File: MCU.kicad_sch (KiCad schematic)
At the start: 45 parts, among them J15 Conn_01x08, J16 Conn_02x04_Odd_Even, J17 TFC-103-01-F-D, J19 TFC-103-01-F-D, Q13 SI2300, SW1 SW_Push_Dual, SW2 SW_Push_Dual, SW3 SW_DIP_x08, U15 MCP1700-3302E_SOT23, U16 CD74HC4067M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

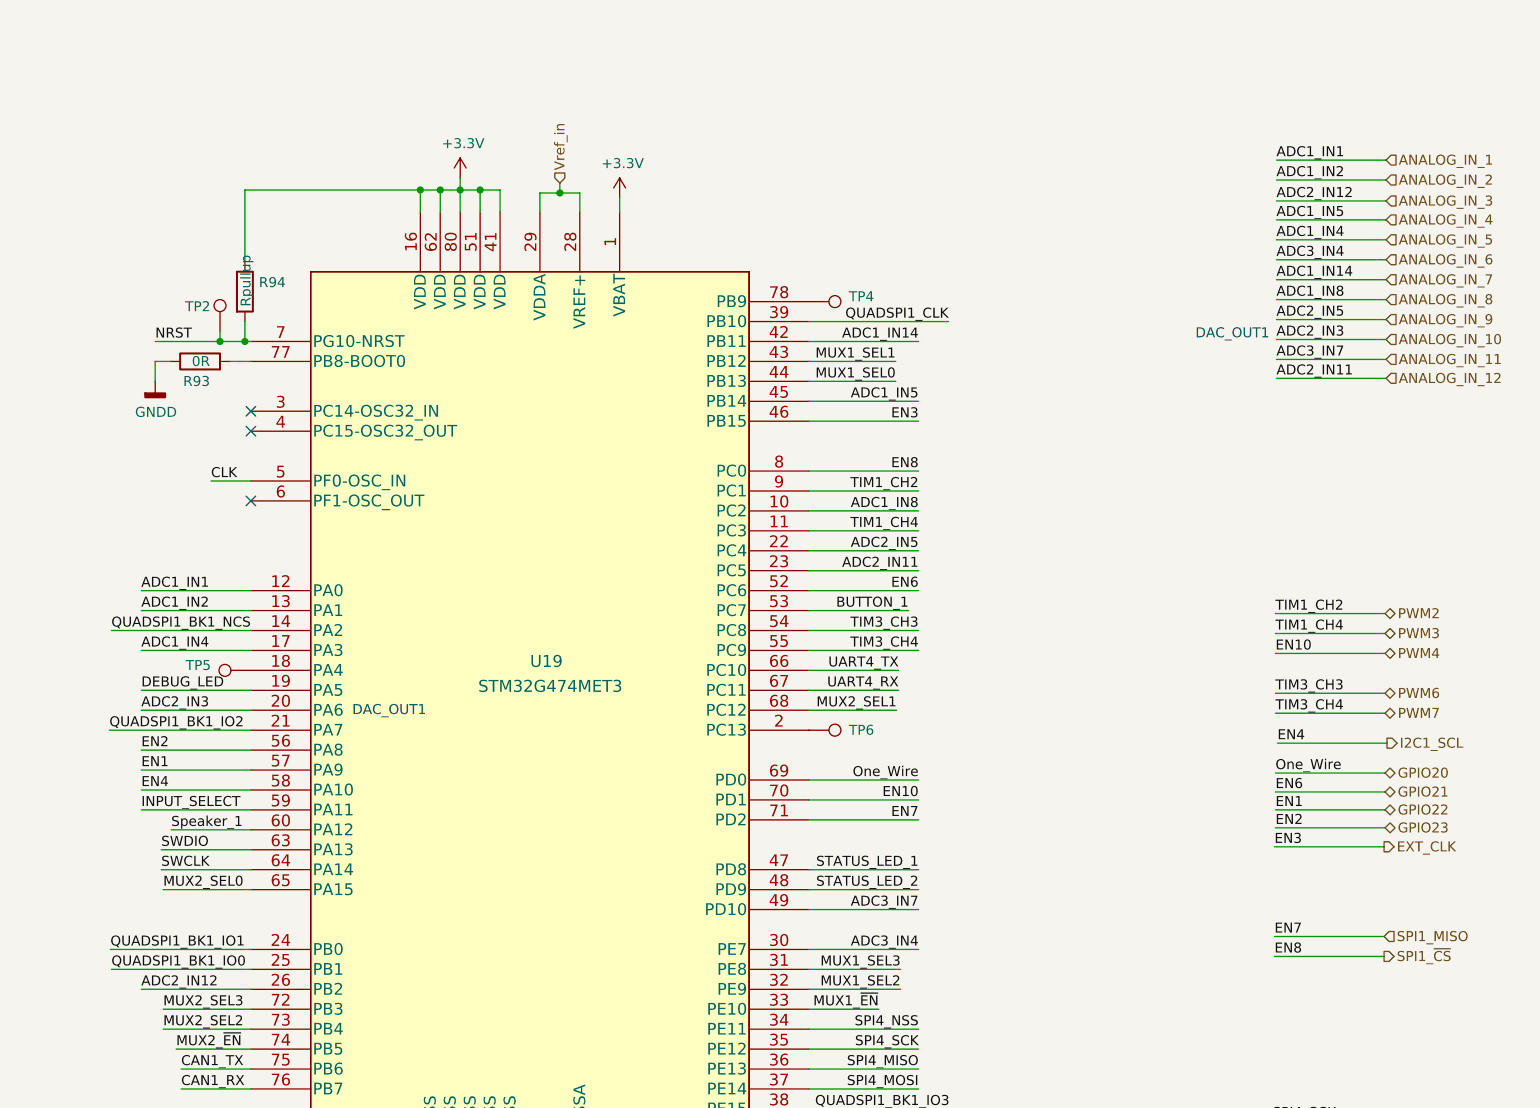
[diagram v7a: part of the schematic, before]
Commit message: Routing complete. Stitching missing
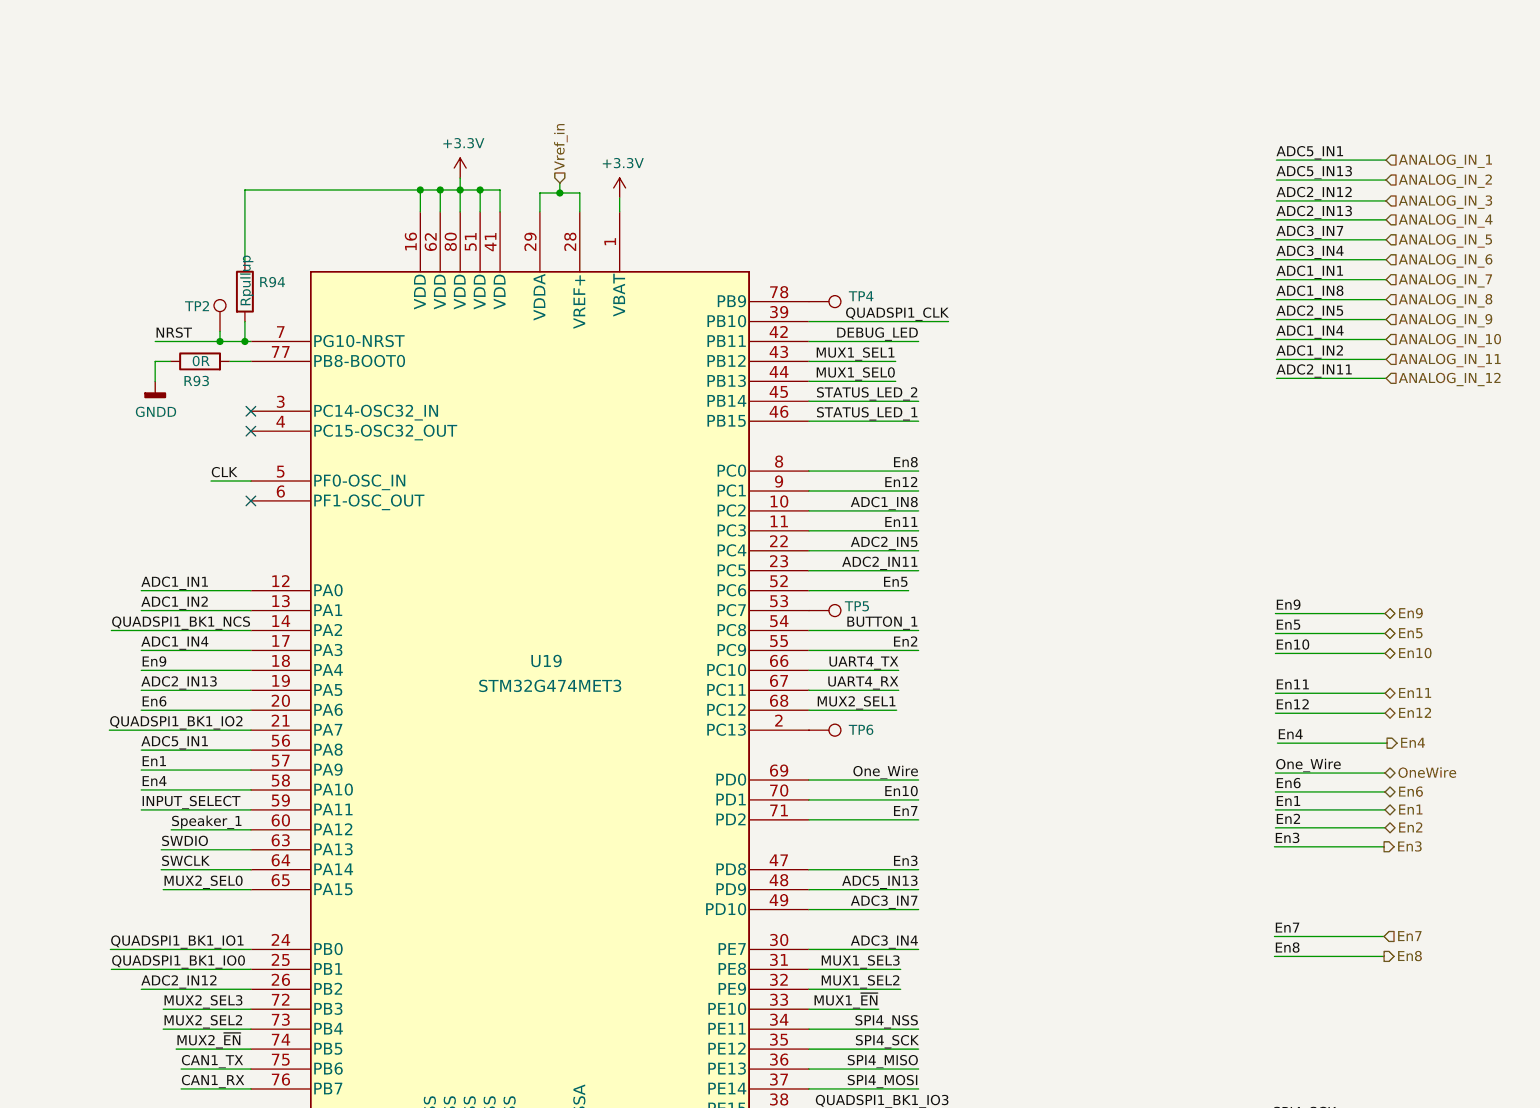
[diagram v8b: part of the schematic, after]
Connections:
- net EXT_CLK is gone; now on net STATUS_LED_1: U19.46 (PB15)
- net GPIO23 is gone; now on net ANALOG_IN_1: U19.56 (PA8)
- net PWM6 is gone; now on net BUTTON_1: U19.54 (PC8)
- net ANALOG_IN_1: no longer U19.12 (PA0)
- net ANALOG_IN_10: now also U19.17 (PA3); no longer U19.20 (PA6)
- net ANALOG_IN_11: now also U19.13 (PA1); no longer U19.49 (PD10)
- net ANALOG_IN_2: now also U19.48 (PD9); no longer U19.13 (PA1)
- net ANALOG_IN_4: now also U19.19 (PA5); no longer U19.45 (PB14)
- net ANALOG_IN_5: now also U19.49 (PD10); no longer U19.17 (PA3)
- net ANALOG_IN_7: now also U19.12 (PA0); no longer U19.42 (PB11)
- net BUTTON_1: no longer U19.53 (PC7)
- net DEBUG_LED: now also U19.42 (PB11); no longer U19.19 (PA5)
- net STATUS_LED_1: no longer U19.47 (PD8)
- net STATUS_LED_2: now also U19.45 (PB14); no longer U19.48 (PD9)
- net at TP5.1: now also U19.53 (PC7); no longer U19.18 (PA4)
- net GPIO20 renamed OneWire
- net GPIO21 renamed En5
- net GPIO22 renamed En1
- net I2C1_SCL renamed En4
- net PWM2 renamed En12
- net PWM3 renamed En11
- net PWM4 renamed En10
- net PWM7 renamed En2
- net SPI1_MISO renamed En7
- net SPI1_~{CS} renamed En8
- new net En3: U19.47 (PD8)
- new net En6: U19.20 (PA6)
- new net En9: U19.18 (PA4)
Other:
- note removed: "DAC_OUT1"
